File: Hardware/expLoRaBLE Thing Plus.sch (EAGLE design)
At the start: 70 parts, among them J2 CORTEX_DEBUG, J5 USB Female Type C Connector, J6 QWIIC_RIGHT_ANGLE, J8 U.FL, U1 MCP73831, U2 3.3V, U3 NM180100, U4 CH340E_MSOP10, U6 DPX202700DT-4162A1, Y1 32.768kHz

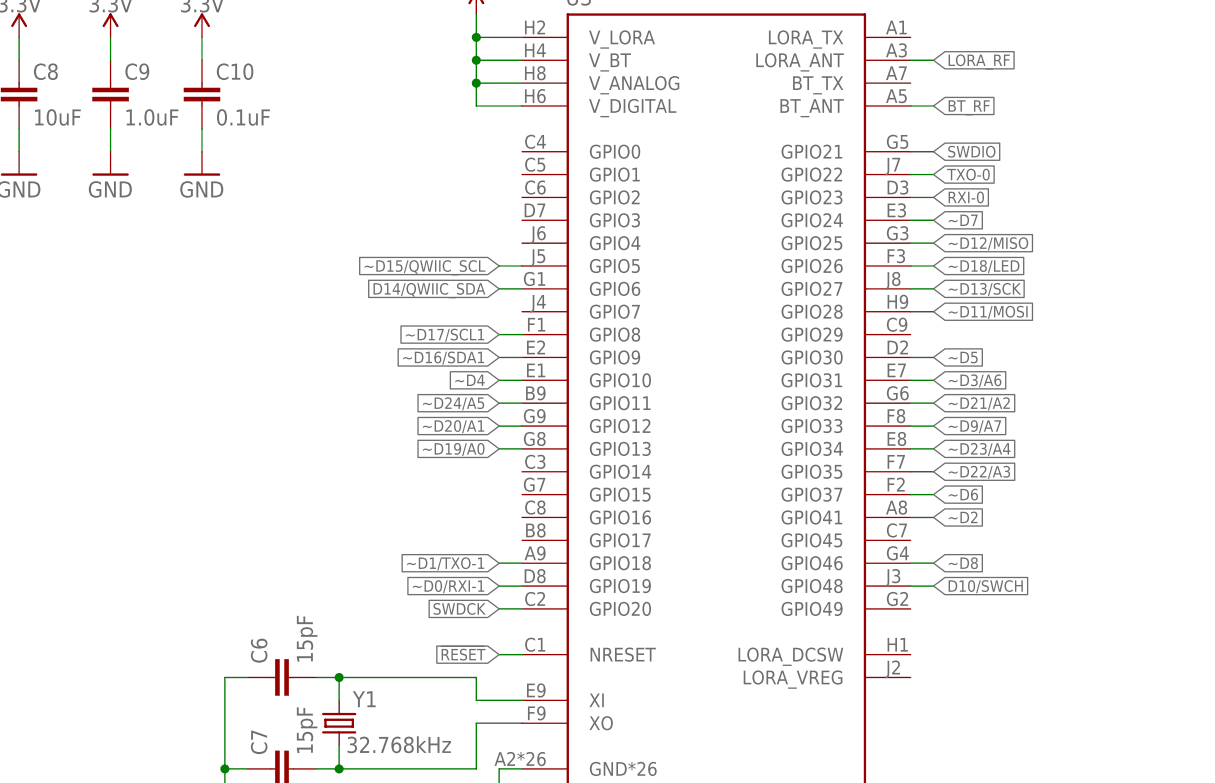
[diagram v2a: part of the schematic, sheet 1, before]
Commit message: UART pin change
-changed UART pin selection to match "standard" sparkfun SVL bootloader
-TXO:GPIO48, RXI:GPIO49
-Note, also moved "D10" net/button to GPIO4. This will also need to be configured with a custom "info zero" file to configure ASB to work.
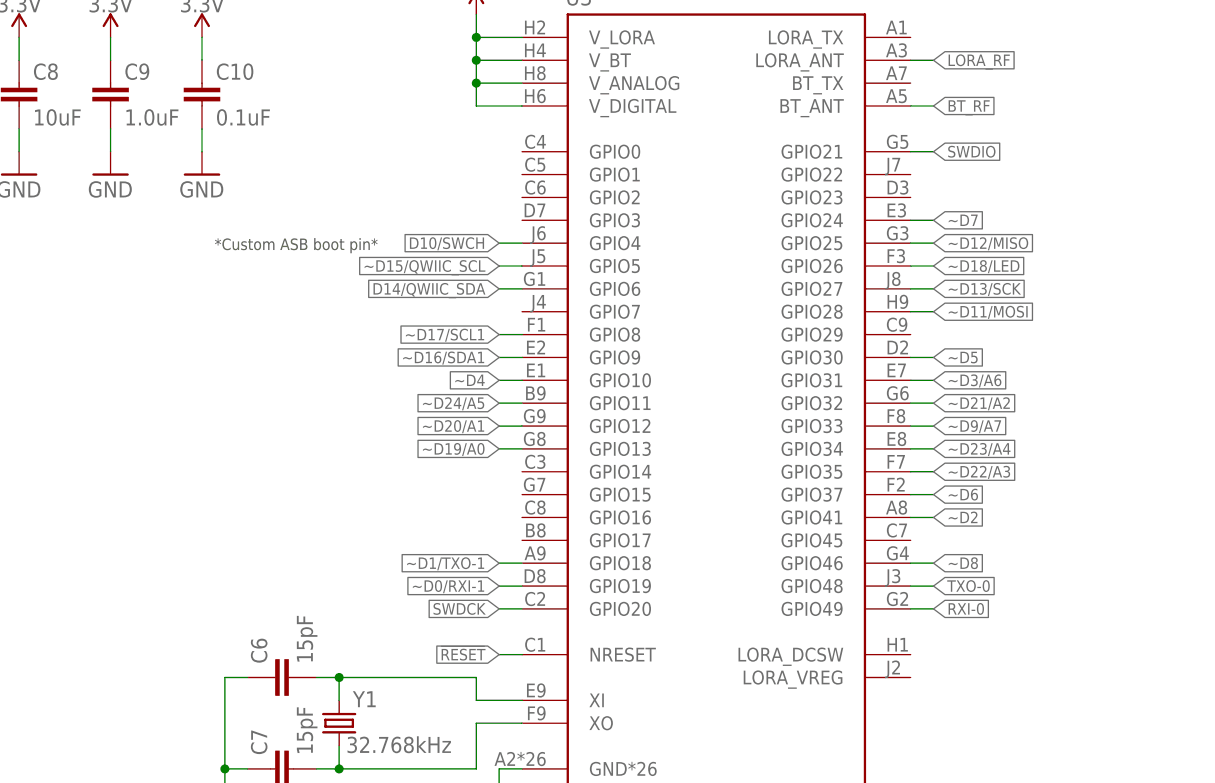
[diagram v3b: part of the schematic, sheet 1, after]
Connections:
- net D10/SWCH: now also U3.GPIO4; no longer U3.GPIO48
- net RXI-0: now also U3.GPIO49; no longer U3.GPIO23
- net TXO-0: now also U3.GPIO48; no longer U3.GPIO22
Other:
- note added: "*Custom ASB boot pin*"
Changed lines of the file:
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@@
 <wire x1="216.408" y1="162.306" x2="208.28" y2="144.272" width="0.1524" layer="97" style="shortdash"/>
 <text x="2.54" y="127" size="1.778" layer="97" font="vector">VCC Range: 2.8-3.6V</text>
+<text x="47.498" y="94.488" size="1.27" layer="97" rot="R180">*Custom ASB boot pin*</text>
 </plain>
 <instances>
@@
 <net name="RXI-0" class="0">
 <segment>
-<wire x1="106.68" y1="99.06" x2="109.22" y2="99.06" width="0.1524" layer="91"/>
-<label x="109.22" y="99.06" size="1.27" layer="95" font="vector" xref="yes"/>
-<pinref part="U3" gate="G$1" pin="GPIO23"/>
+<wire x1="106.68" y1="53.34" x2="109.22" y2="53.34" width="0.1524" layer="91"/>
+<label x="109.22" y="53.34" size="1.27" layer="95" font="vector" xref="yes"/>
+<pinref part="U3" gate="G$1" pin="GPIO49"/>
 </segment>
 </net>
 <net name="TXO-0" class="0">
 <segment>
-<wire x1="106.68" y1="101.6" x2="109.22" y2="101.6" width="0.1524" layer="91"/>
-<label x="109.22" y="101.6" size="1.27" layer="95" font="vector" xref="yes"/>
-<pinref part="U3" gate="G$1" pin="GPIO22"/>
+<wire x1="106.68" y1="55.88" x2="109.22" y2="55.88" width="0.1524" layer="91"/>
+<label x="109.22" y="55.88" size="1.27" layer="95" font="vector" xref="yes"/>
+<pinref part="U3" gate="G$1" pin="GPIO48"/>
 </segment>
 </net>
@@
 <net name="D10/SWCH" class="0">
 <segment>
-<wire x1="106.68" y1="55.88" x2="109.22" y2="55.88" width="0.1524" layer="91"/>
-<label x="109.22" y="55.88" size="1.27" layer="95" font="vector" xref="yes"/>
-<pinref part="U3" gate="G$1" pin="GPIO48"/>
-</segment>
-</net>
+<wire x1="63.5" y1="93.98" x2="60.96" y2="93.98" width="0.1524" layer="91"/>
+<label x="60.96" y="93.98" size="1.27" layer="95" font="vector" rot="R180" xref="yes"/>
+<pinref part="U3" gate="G$1" pin="GPIO4"/>
+</segment>
+</net>

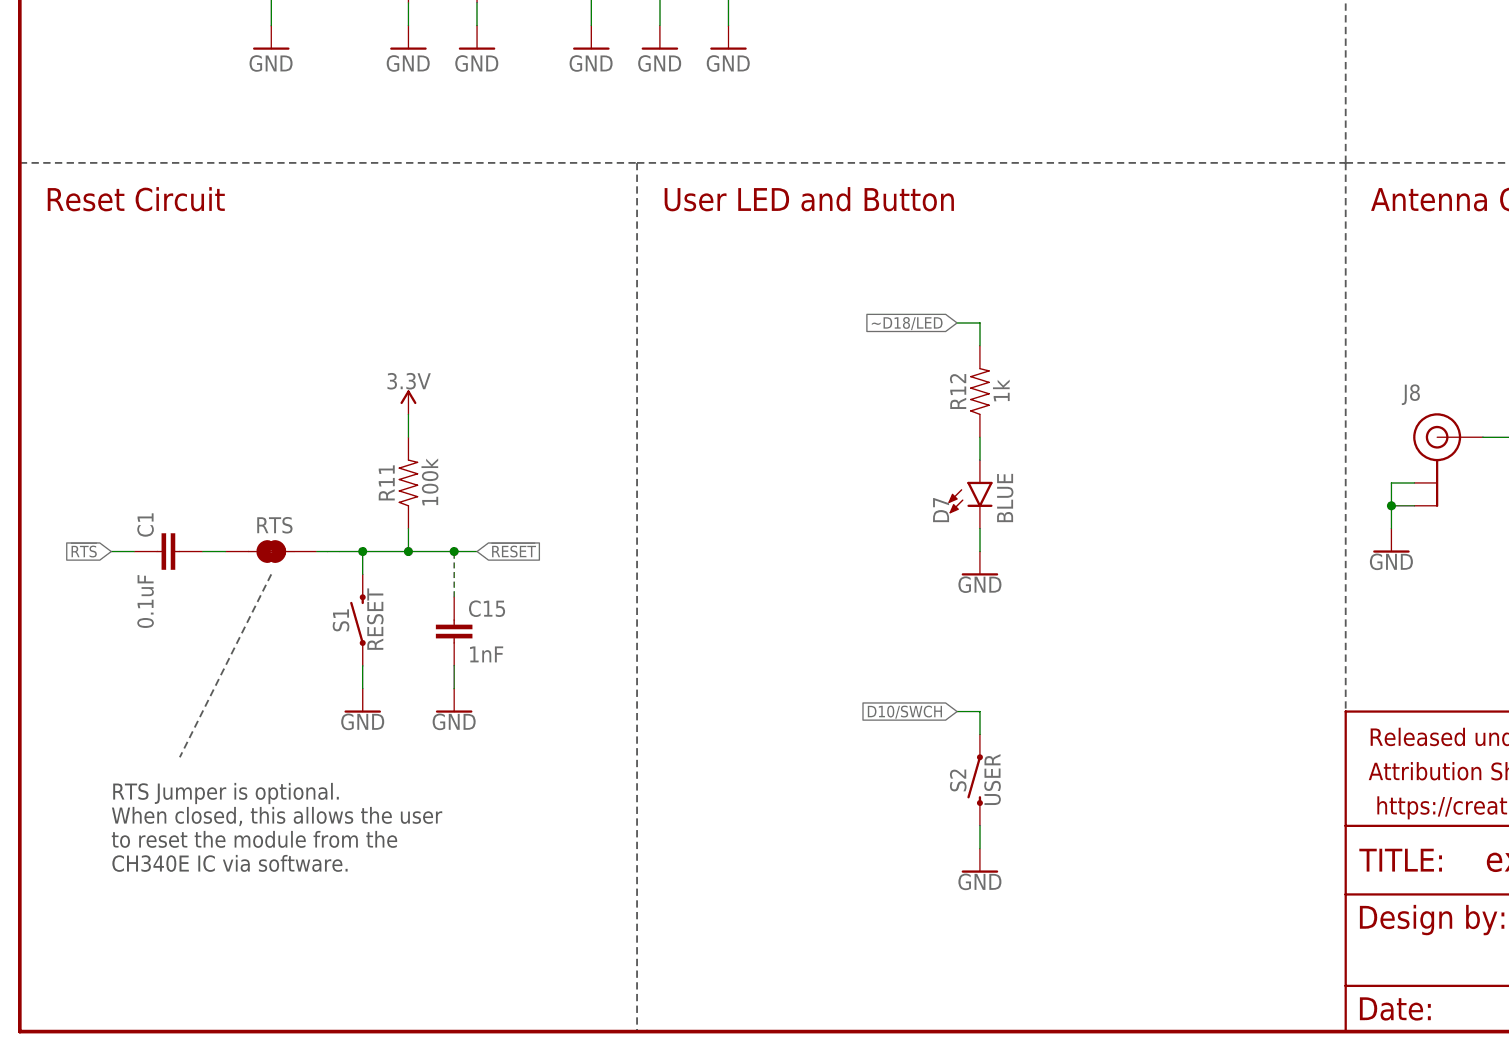
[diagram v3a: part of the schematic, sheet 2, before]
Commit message: Added Boot net/pin (for ASB)
-chose a boot pin (GPIO22). Note, we could not use the standard SFE pin of GPIO47, but this can be set during production programming of custom "info.0" binary.
-connected RTS (post closed jumper) to boot net, including C13 and pull down R10.
-left D10 on GPIO4 and is separate from boot circuit. It is soley a user button, similar to the Artemis Thing Plus design (although on a different GPIO#).
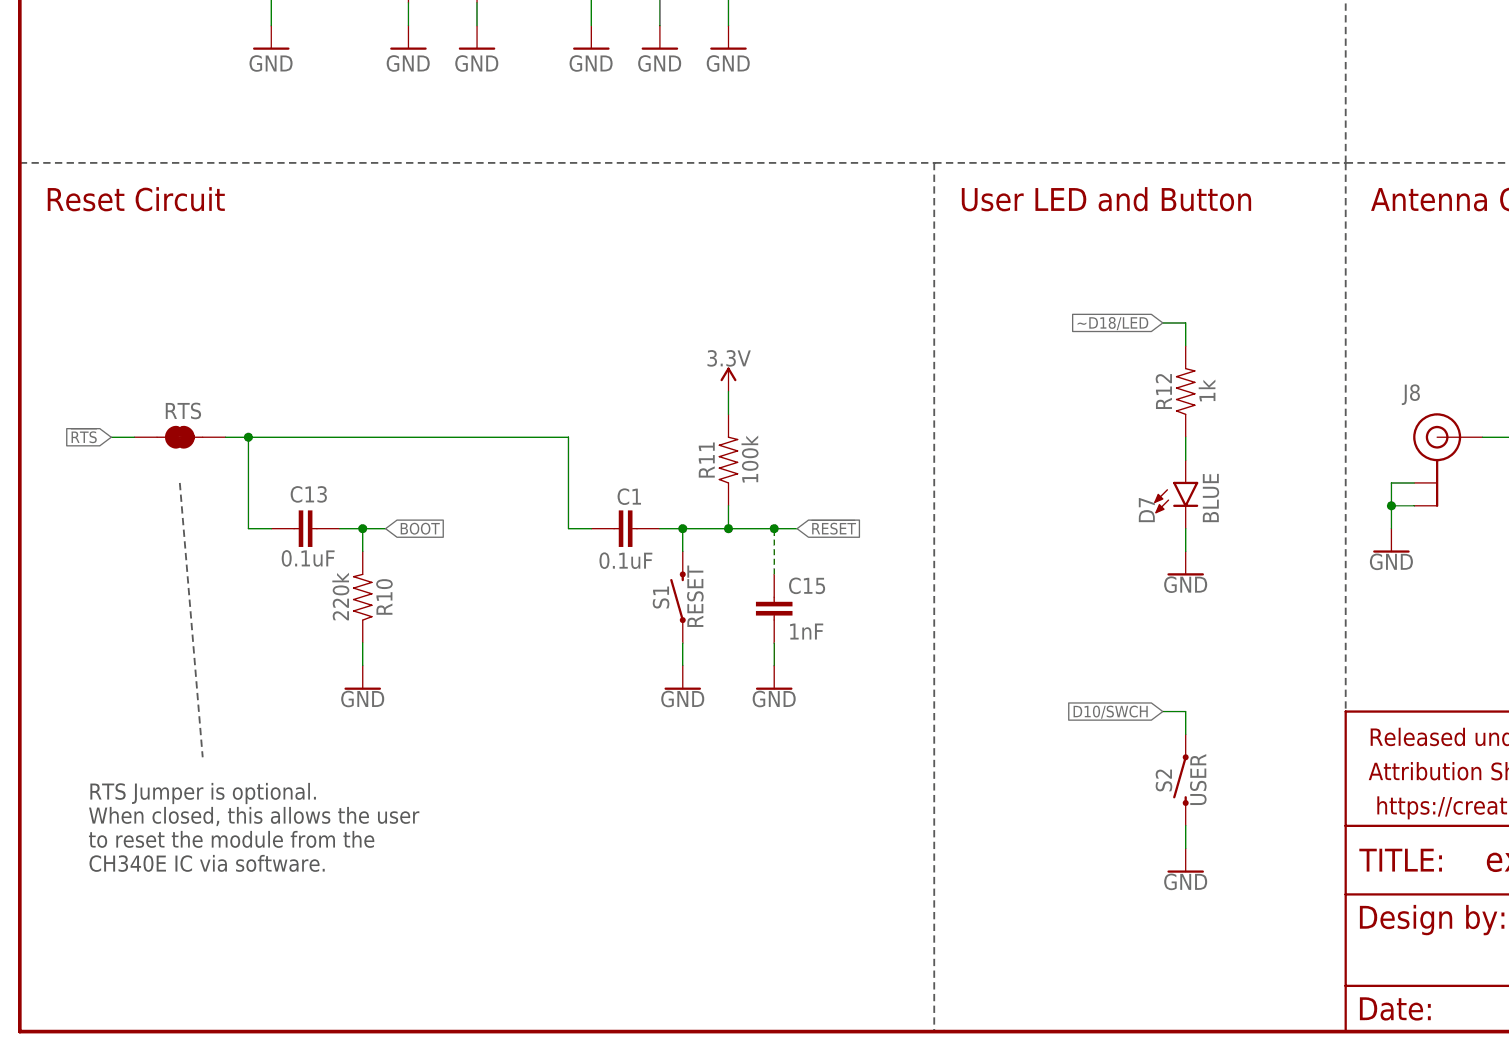
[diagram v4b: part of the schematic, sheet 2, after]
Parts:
- added C13: 0.1uF, SparkFun-Capacitors:0.1UF-0603-25V-5%
- added R10: 220k, SparkFun-Resistors:220KOHM-0603-1/10W-1%
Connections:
- new net BOOT: C13.2, R10.2, U3.GPIO22
- net !RESET: now also C1.2; no longer RTS.2
- net !RTS: now also RTS.1; no longer C1.1
- net GND: now also R10.1
- net N$15: now also C1.1, C13.1, RTS.2; no longer C1.2, RTS.1
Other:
- note added: "*Unique boot pin* Most other SFE Apollo boards use GPIO47"
- note removed: "*Custom ASB boot pin*"
- moved on the sheet: C1, C15, D7, R11, R12, RTS, S1, S2

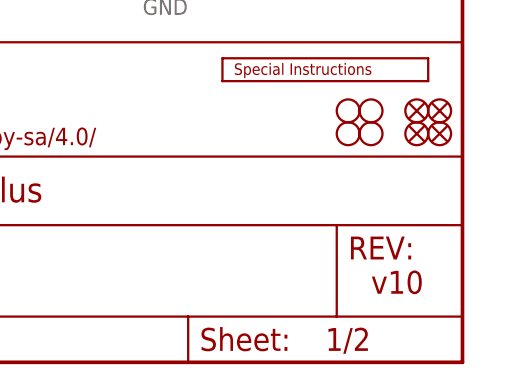
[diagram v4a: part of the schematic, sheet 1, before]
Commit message: Eng Run of Checklist v11
-vector fonts in sch corrected
-updated version number in sheet 2 of sch
-fixed text overlap on qwiic ra connector value text object
-changed 1 0.1uF cap to same version (aka PROD_ID) as others to consolodate BOM
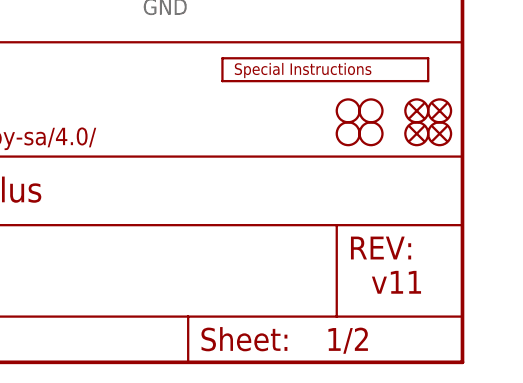
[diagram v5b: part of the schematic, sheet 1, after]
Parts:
- C13: device SparkFun-Capacitors:0.1UF-0603-25V-5% -> SparkFun-Capacitors:0.1UF-0603-25V-(+80/-20%)
- J6: value QWIIC_RIGHT_ANGLE -> QWIIC_RA
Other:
- note removed: "v10"
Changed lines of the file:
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@@
 <part name="D7" library="SparkFun-LED" library_urn="urn:adsk.eagle:library:529" deviceset="LED-BLUE" device="0603" package3d_urn="urn:adsk.eagle:package:23926016/2" value="BLUE"/>
 <part name="GND8" library="SparkFun-PowerSymbols" deviceset="GND" device=""/>
-<part name="J6" library="SparkFun-Connectors" deviceset="QWIIC_CONNECTOR" device="JS-1MM" override_package3d_urn="urn:adsk.eagle:package:23933495/2" override_package_urn="urn:adsk.eagle:footprint:23933496/1" value="QWIIC_RIGHT_ANGLE"/>
+<part name="J6" library="SparkFun-Connectors" deviceset="QWIIC_CONNECTOR" device="JS-1MM" override_package3d_urn="urn:adsk.eagle:package:23933495/2" override_package_urn="urn:adsk.eagle:footprint:23933496/1" value="QWIIC_RA"/>
 <part name="GND3" library="SparkFun-PowerSymbols" deviceset="GND" device=""/>
 <part name="SUPPLY5" library="SparkFun-PowerSymbols" deviceset="3.3V" device=""/>
@@
 <part name="GND41" library="SparkFun-PowerSymbols" deviceset="GND" device=""/>
 <part name="R10" library="SparkFun-Resistors" deviceset="220KOHM" device="-0603-1/10W-1%" value="220k"/>
-<part name="C13" library="SparkFun-Capacitors" deviceset="0.1UF" device="-0603-25V-5%" value="0.1uF"/>
+<part name="C13" library="SparkFun-Capacitors" deviceset="0.1UF" device="-0603-25V-(+80/-20%)" value="0.1uF"/>
 </parts>
 <sheets>
@@
 <text x="193.04" y="174.498" size="1.778" layer="97" font="vector">VIN: 6V Max</text>
 <text x="168.656" y="11.43" size="2.54" layer="94" font="vector">Daniel Dobre</text>
-<text x="238.76" y="7.62" size="2.54" layer="94" font="vector">v10</text>
+<text x="238.76" y="7.62" size="2.54" layer="94" font="vector">v11</text>
 <text x="222.25" y="179.07" size="1.778" layer="97" font="vector">Cut LED jumper
 to disable power LED</text>
@@
 <wire x1="216.408" y1="162.306" x2="208.28" y2="144.272" width="0.1524" layer="97" style="shortdash"/>
 <text x="2.54" y="127" size="1.778" layer="97" font="vector">VCC Range: 2.8-3.6V</text>
-<text x="144.272" y="113.284" size="1.27" layer="97" rot="R180">*Unique boot pin*
+<text x="144.272" y="113.284" size="1.27" layer="97" font="vector" rot="R180">*Unique boot pin*
 Most other SFE Apollo
 boards use GPIO47</text>
